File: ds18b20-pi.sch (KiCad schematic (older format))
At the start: 12 parts, among them J1 Conn_01x03_Female, J10 Conn_01x03_Female, J2 Conn_01x03_Female, J3 Conn_01x03_Female, J4 Conn_01x03_Female, J5 Conn_01x03_Female, J6 Conn_01x03_Female, J7 Conn_01x03_Female, J8 Conn_01x03_Female, J9 Conn_01x03_Female, P1 CONN_13X2

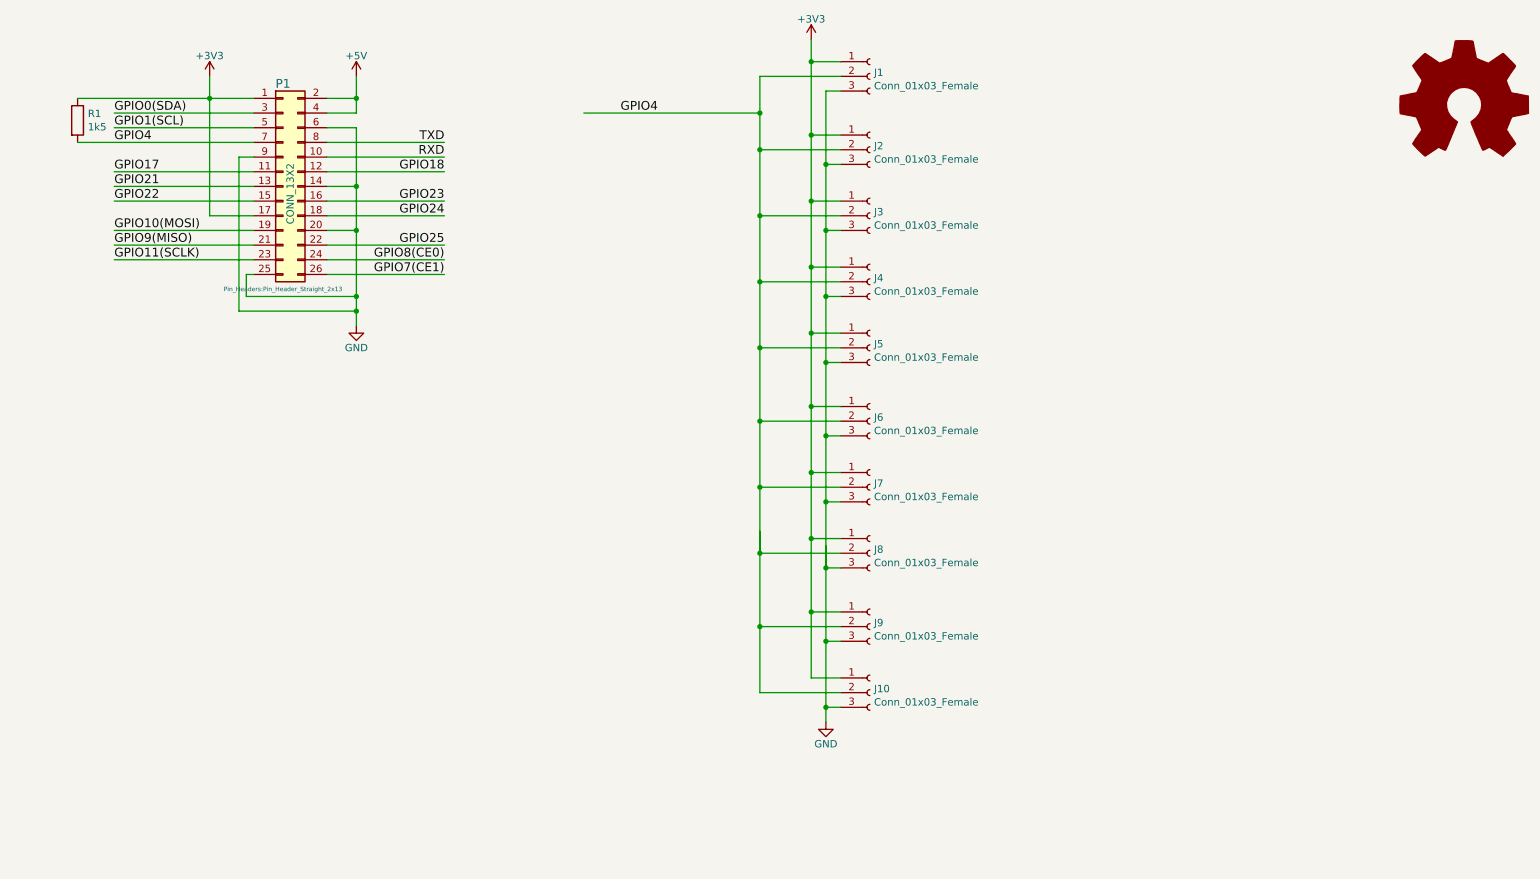
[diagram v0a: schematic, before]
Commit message: Less GPIO4 more relays for motors
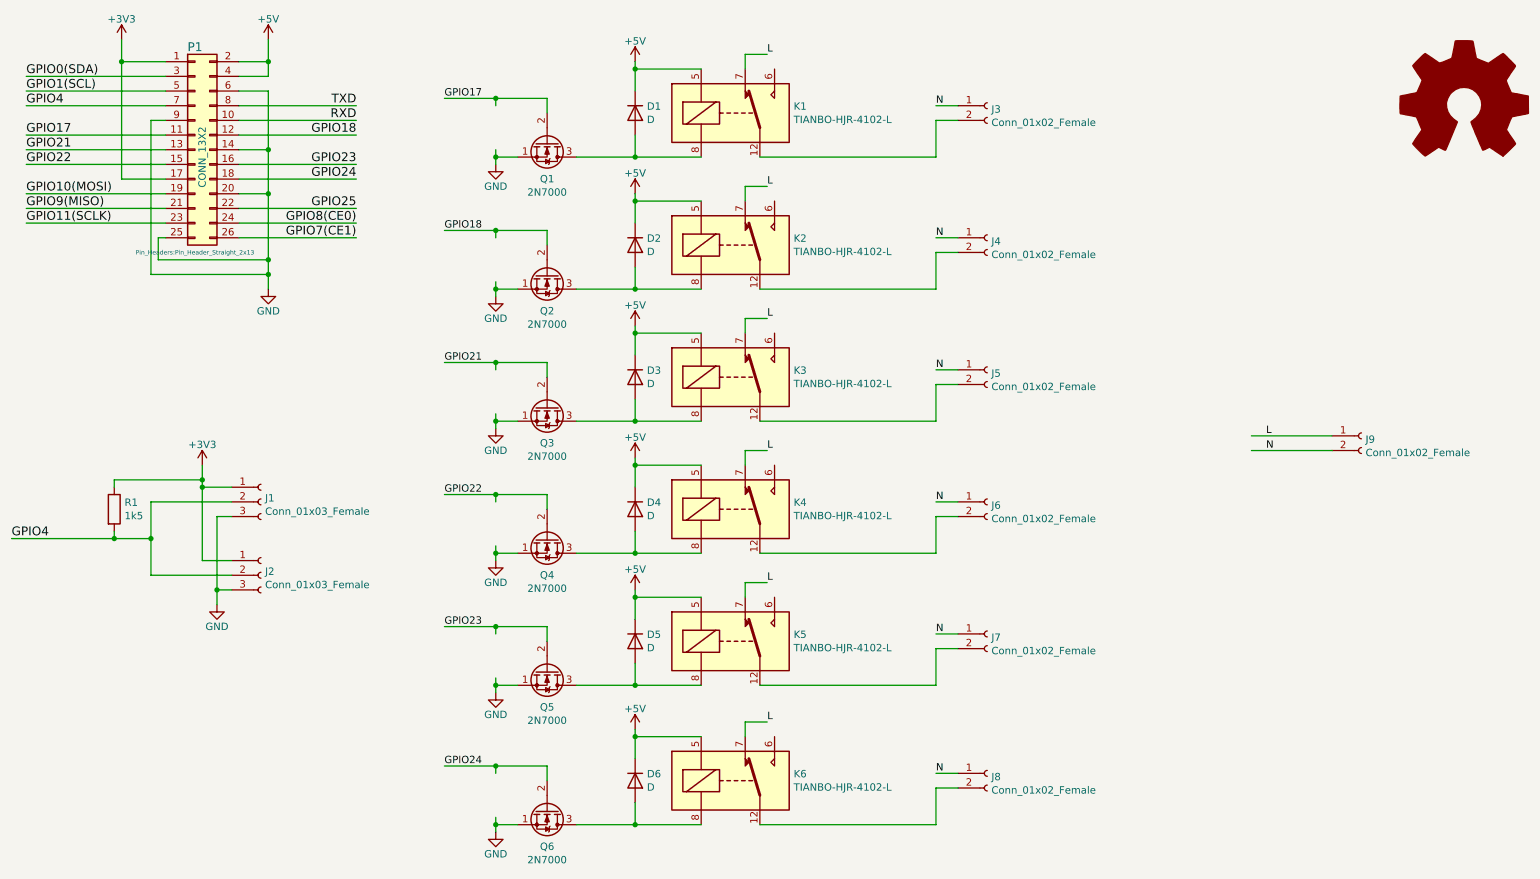
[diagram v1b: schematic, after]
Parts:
- removed J10, J3, J4, J5, J6, J7, J8, J9: Conn_01x03_Female, Connector_Phoenix_MC:PhoenixContact_MC_1,5_3-G-3.5_1x03_P3.50mm_Horizontal, symbol Connector:Conn_01x03_Female
- added D1, D2, D3, D4, D5, D6: D, Diode_THT:D_DO-35_SOD27_P7.62mm_Horizontal, symbol Device:D
- added J3, J4, J5, J6, J7, J8, J9: Conn_01x02_Female, Connector_Phoenix_MC:PhoenixContact_MC_1,5_2-G-3.5_1x02_P3.50mm_Horizontal, symbol Connector:Conn_01x02_Female
- added K1, K2, K3, K4, K5, K6: TIANBO-HJR-4102-L, Relay_THT:Relay_SPDT_HJR-4102, symbol Relay:TIANBO-HJR-4102-L
- added Q1, Q2, Q3, Q4, Q5, Q6: 2N7000, Package_TO_SOT_THT:TO-92_Inline, symbol Transistor_FET:2N7000
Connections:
- net labels added: L, N
- wire segments 103 -> 173
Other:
- moved on the sheet: J1, J2, P1, R1
